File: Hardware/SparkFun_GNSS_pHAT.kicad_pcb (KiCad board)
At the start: 4 copper layers, 65 x 56.8 mm, 147 parts, among them J1 Raspberry_Pi_2x20_SMD_Passthr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, J2 Conn_02x10, J3 U.FL, J4 Conn_02x10, J5 microSD_Friction, J6 USB_C_Receptacle, J7 SMA_Edge, J8 Qwiic_Vertical, J9 Conn_01x05, U1 CAT24C512WI-GT3, U2 AP7361C-3.3V, U3 RT9080-3.3

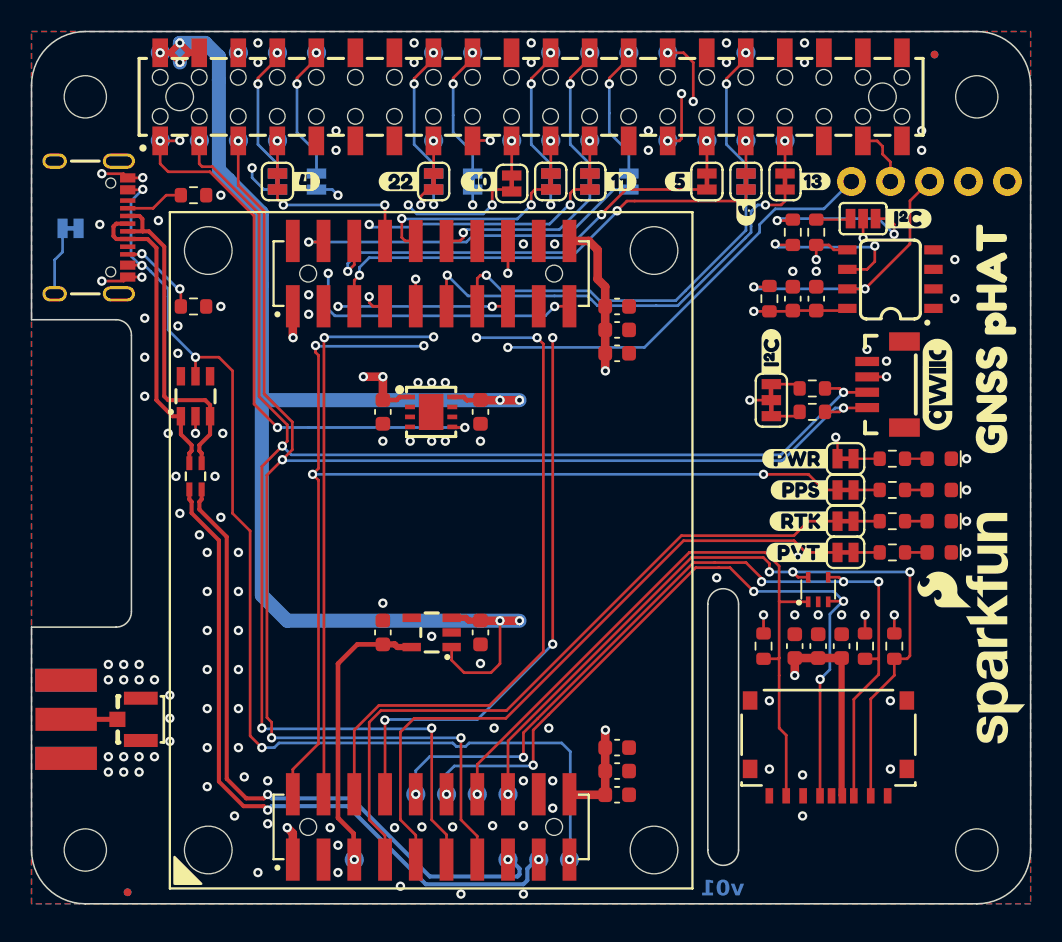
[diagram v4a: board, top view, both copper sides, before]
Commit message: v10 - update connectors and silk
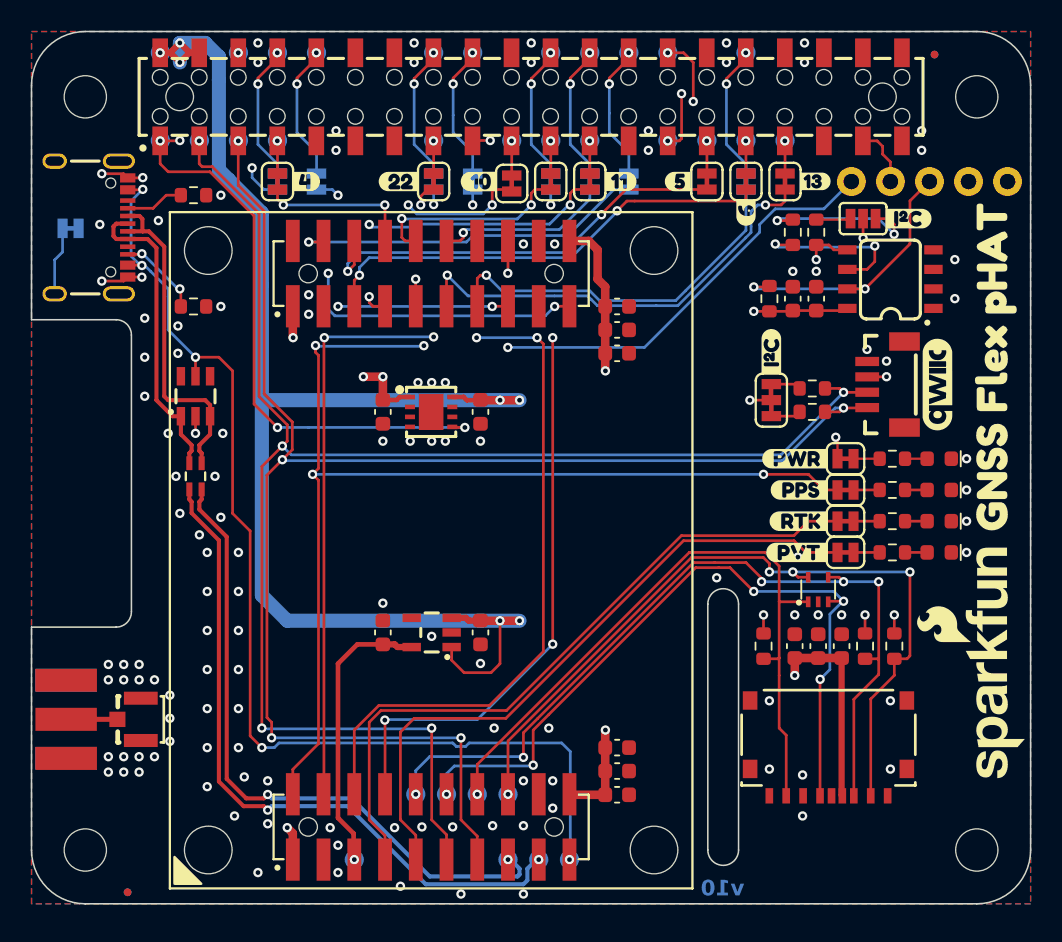
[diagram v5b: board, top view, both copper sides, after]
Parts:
- removed kibuzzard-67922B7F: G***, kibuzzard-67922B7F
- removed kibuzzard-67923C07: G***, kibuzzard-67923C07
- added Ref**: Val**, SparkFun-Aesthetic:OSHW_Logo_5mm, B.Cu at (147.7, 109.9)
- added kibuzzard-67DC1838: G***, kibuzzard-67DC1838, F.Cu at (178.3, 89.5)
- added kibuzzard-67DC18B6: G***, kibuzzard-67DC18B6, B.Cu at (147.7, 102.4)
- J2, J4: footprint SparkFun-Connector:2x10_2.0mm_Male_Pins_Vertical_SMD -> SparkFun-Connector:2x10_2.0mm_Male_Pins_Vertical_SMD_Pegs
- moved G*** 2.26 mm to (178.1, 109.0)
- moved G*** 0.31 mm to (148.5, 96.5)
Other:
- board text added: "v10"
- board text removed: "v01"
